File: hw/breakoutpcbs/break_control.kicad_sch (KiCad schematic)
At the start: 21 parts, among them J11 Conn_01x07, J12 Conn_01x07, J13 Conn_01x06, J15 Conn_01x04, J16 Screw_Terminal_01x04, J17 Conn_01x05, J18 Screw_Terminal_01x04, Q10 BC337, Q11 BC847

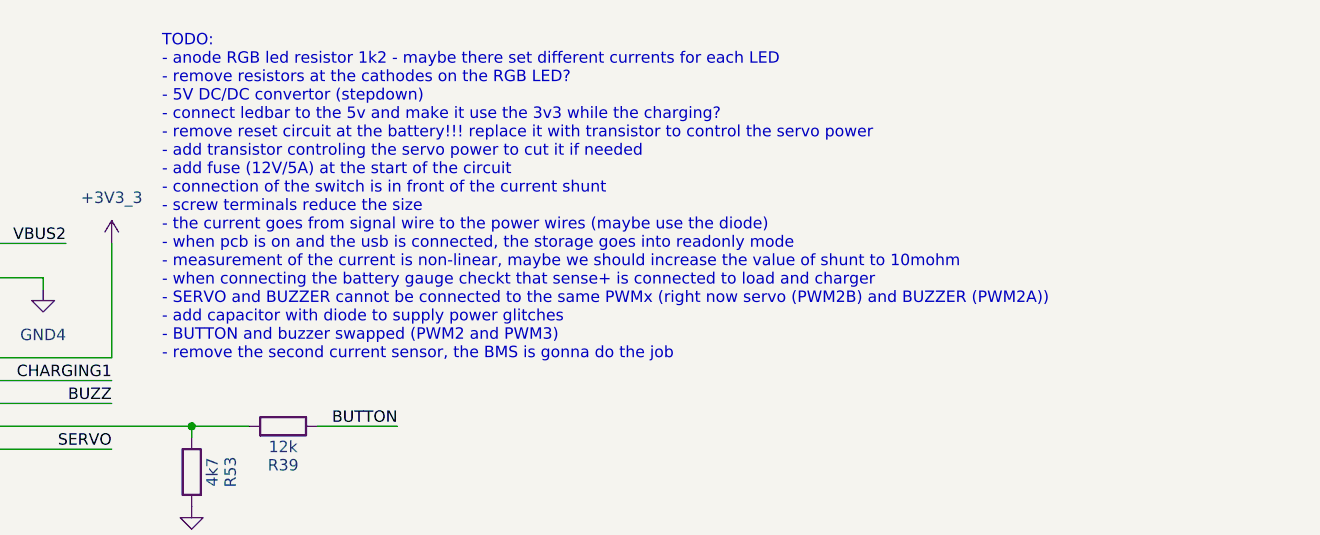
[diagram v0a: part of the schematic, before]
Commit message: new todos, the charging signal removed, plugged signal used instead
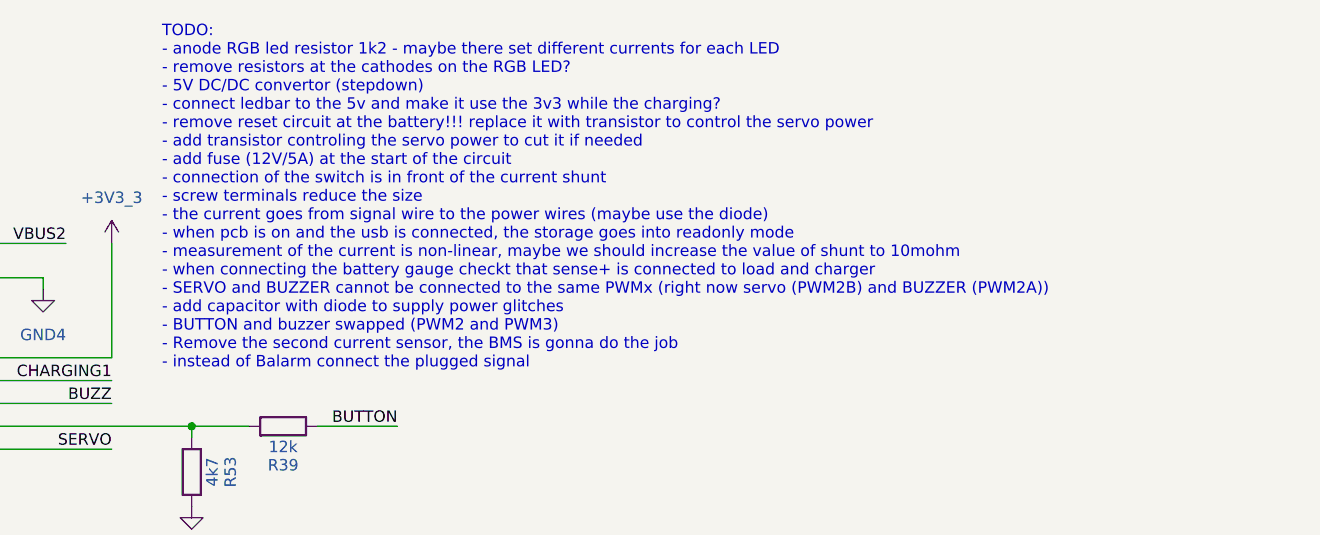
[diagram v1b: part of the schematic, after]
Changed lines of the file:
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@@
 		)
 	)
-	(text "TODO: \n- anode RGB led resistor 1k2 - maybe there set different currents for each LED\n- remove resistors at the cathodes on the RGB LED?\n- 5V DC/DC convertor (stepdown)\n- connect ledbar to the 5v and make it use the 3v3 while the charging?\n- remove reset circuit at the battery!!! replace it with transistor to control the servo power\n- add transistor controling the servo power to cut it if needed\n- add fuse (12V/5A) at the start of the circuit\n- connection of the switch is in front of the current shunt\n- screw terminals reduce the size\n- the current goes from signal wire to the power wires (maybe use the diode)\n- when pcb is on and the usb is connected, the storage goes into readonly mode\n- measurement of the current is non-linear, maybe we should increase the value of shunt to 10mohm\n- when connecting the battery gauge checkt that sense+ is connected to load and charger\n- SERVO and BUZZER cannot be connected to the same PWMx (right now servo (PWM2B) and BUZZER (PWM2A))\n- add capacitor with diode to supply power glitches\n- BUTTON and buzzer swapped (PWM2 and PWM3)\n- remove the second current sensor, the BMS is gonna do the job"
+	(text "TODO: \n- anode RGB led resistor 1k2 - maybe there set different currents for each LED\n- remove resistors at the cathodes on the RGB LED?\n- 5V DC/DC convertor (stepdown)\n- connect ledbar to the 5v and make it use the 3v3 while the charging?\n- remove reset circuit at the battery!!! replace it with transistor to control the servo power\n- add transistor controling the servo power to cut it if needed\n- add fuse (12V/5A) at the start of the circuit\n- connection of the switch is in front of the current shunt\n- screw terminals reduce the size\n- the current goes from signal wire to the power wires (maybe use the diode)\n- when pcb is on and the usb is connected, the storage goes into readonly mode\n- measurement of the current is non-linear, maybe we should increase the value of shunt to 10mohm\n- when connecting the battery gauge checkt that sense+ is connected to load and charger\n- SERVO and BUZZER cannot be connected to the same PWMx (right now servo (PWM2B) and BUZZER (PWM2A))\n- add capacitor with diode to supply power glitches\n- BUTTON and buzzer swapped (PWM2 and PWM3)\n- Remove the second current sensor, the BMS is gonna do the job\n- instead of Balarm connect the plugged signal\n"
 		(exclude_from_sim no)
 		(at 173.228 33.02 0)
